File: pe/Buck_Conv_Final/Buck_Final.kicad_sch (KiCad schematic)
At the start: 11 parts, among them U1 BD95821MUV-E2

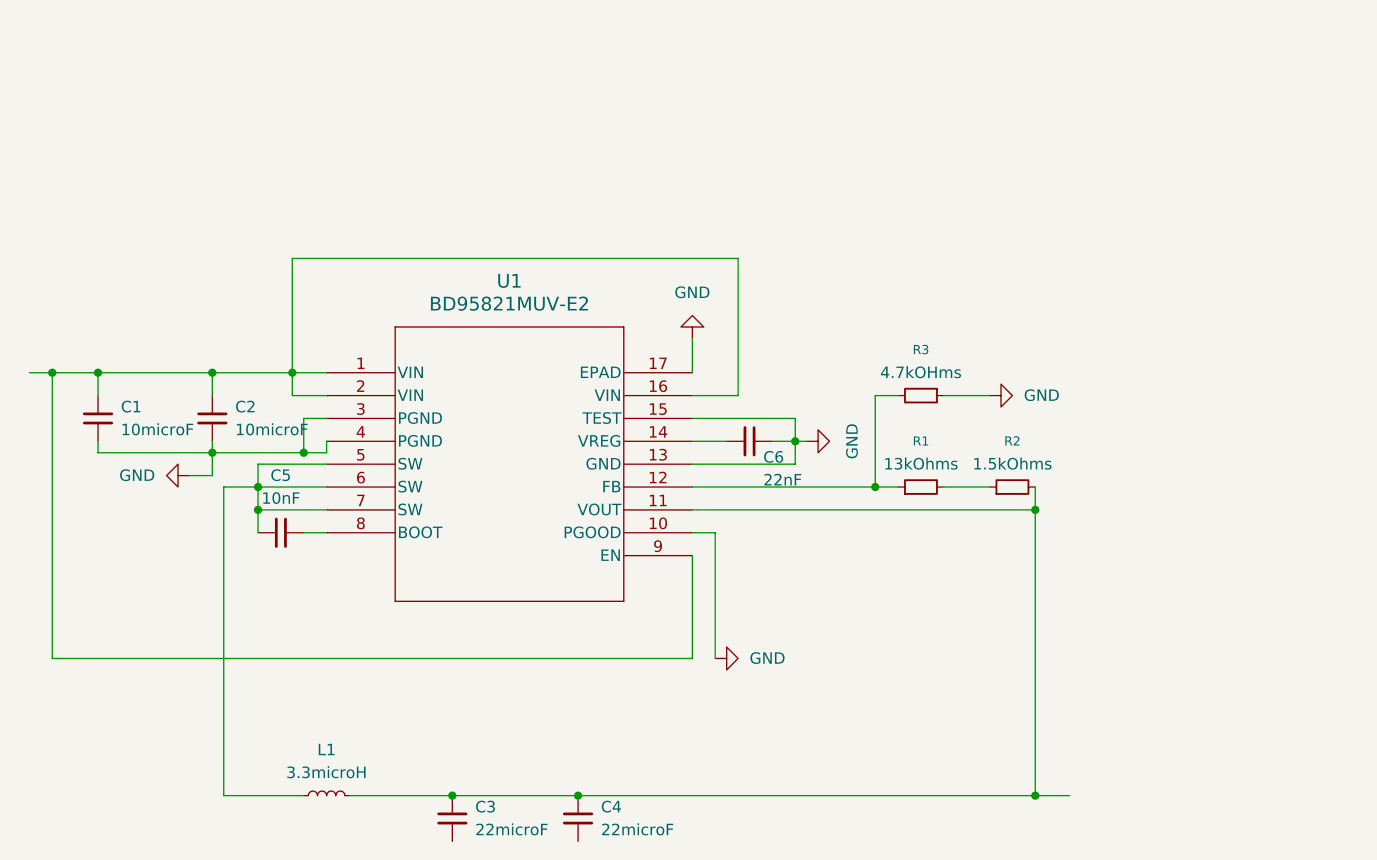
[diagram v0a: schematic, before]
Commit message: Buck Conv with TPS5405
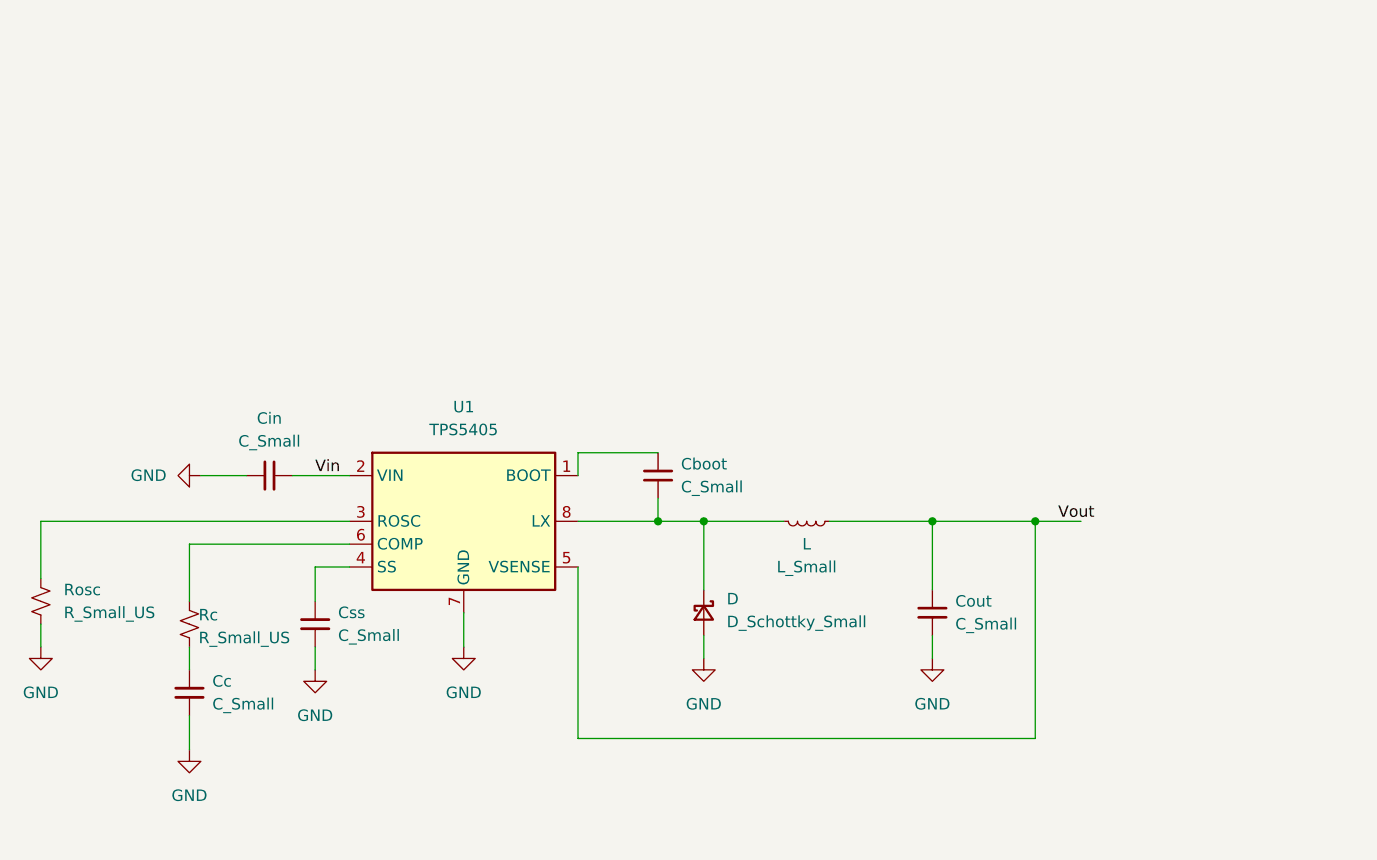
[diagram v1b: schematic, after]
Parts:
- removed C1, C2: 10microF, symbol Device:C_Small
- removed C3, C4: 22microF, symbol Device:C_Small
- removed C5: 10nF, symbol Device:C_Small
- removed C6: 22nF, symbol Device:C_Small
- removed L1: 3.3microH, symbol Device:L_Small
- removed R1: 13kOhms, symbol Device:R_Small
- removed R2: 1.5kOhms, symbol Device:R_Small
- removed R3: 4.7kOHms, symbol Device:R_Small
- removed U1: BD95821MUV-E2, BD95821MUV:VQFN016V3030_ROM, symbol BD95821MUV:BD95821MUV-E2
- added Cboot, Cc, Cin, Cout, Css: C_Small, symbol Device:C_Small
- added D: D_Schottky_Small, symbol Device:D_Schottky_Small
- added L: L_Small, symbol Device:L_Small
- added Rc, Rosc: R_Small_US, Resistor_THT:R_Array_SIP4, symbol Device:R_Small_US
- added U1: TPS5405, Package_SO:SOIC-8_3.9x4.9mm_P1.27mm, symbol Regulator_Switching:TPS5403
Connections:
- net GND: now also Cc.1, Cin.1, Cout.2, Css.1, D.2 (A), Rosc.2, U1.7 (GND)
- new net: Cboot.1, D.1 (K), L.2, U1.8 (LX)
- new net: Cboot.2, U1.1 (BOOT)
- new net: Rc.1, U1.6 (COMP)
- new net: Cc.2, Rc.2
- new net: Rosc.1, U1.3 (ROSC)
- new net: Css.2, U1.4 (SS)
- new net Vin: Cin.2, U1.2 (VIN)
- new net Vout: Cout.1, L.1, U1.5 (VSENSE)
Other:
- title: Buck Converter -> ${BOARD_TITLE}

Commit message: Schematic Values and PCB Started
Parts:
- removed Cboot, Cc, Cout, Css: C_Small, symbol Device:C_Small
- removed D: D_Schottky_Small, symbol Device:D_Schottky_Small
- removed L: L_Small, symbol Device:L_Small
- removed Rc: R_Small_US, Resistor_THT:R_Array_SIP4, symbol Device:R_Small_US
- removed U1: TPS5405, Package_SO:SOIC-8_3.9x4.9mm_P1.27mm, symbol Regulator_Switching:TPS5403
- added Cboot1: 0.1microF, Capacitor_SMD:C_0603_1608Metric_Pad1.08x0.95mm_HandSolder, symbol Device:C_Small
- added Cc1: 2.2nF, Capacitor_SMD:C_0603_1608Metric_Pad1.08x0.95mm_HandSolder, symbol Device:C_Small
- added Cout1: 100microF, Capacitor_SMD:C_0603_1608Metric_Pad1.08x0.95mm_HandSolder, symbol Device:C_Small
- added Css1: 5nF, Capacitor_SMD:C_0603_1608Metric_Pad1.08x0.95mm_HandSolder, symbol Device:C_Small
- added D1: D_Schottky_Small, Diode_SMD:D_0603_1608Metric_Pad1.05x0.95mm_HandSolder, symbol Device:D_Schottky_Small
- added L1: 10microH, Inductor_SMD:L_0603_1608Metric_Pad1.05x0.95mm_HandSolder, symbol Device:L_Small
- added Rc1: 10kOhms, Resistor_SMD:R_0603_1608Metric_Pad0.98x0.95mm_HandSolder, symbol Device:R_Small_US
- added U2: TPS5405DR, TPS5405DR:D0008A-IPC_A, symbol TPS5405DR:TPS5405DR
- Cin1: renamed from Cin; value C_Small -> 22microF; footprint (none) -> Capacitor_SMD:C_0603_1608Metric_Pad1.08x0.95mm_HandSolder
- Rosc1: renamed from Rosc; value R_Small_US -> 49.9kohms; footprint Resistor_THT:R_Array_SIP4 -> Resistor_SMD:R_0603_1608Metric_Pad0.98x0.95mm_HandSolder
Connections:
- net GND: now also Cc1.1, Cout1.2, Css1.1, D1.2 (A), U2.7 (GND)
- net Vin: now also U2.2 (VIN)
- net Vout: now also Cout1.1, L1.1, U2.5 (VSENSE)
- net at Rosc1.1: now also U2.3 (ROSC)
- new net: Cboot1.1, D1.1 (K), L1.2, U2.8 (LX)
- new net: Rc1.1, U2.6 (COMP)
- new net: Cc1.2, Rc1.2
- new net: Cboot1.2, U2.1 (BOOT)
- new net: Css1.2, U2.4 (SS)
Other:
- title: ${BOARD_TITLE} -> 12-5 Buck Converter
- moved on the sheet: Cin1, Rosc1

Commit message: Diode Rename
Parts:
- D1: value D_Schottky_Small -> (none)
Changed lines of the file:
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@@
 			)
 		)
-		(property "Value" "D_Schottky_Small"
+		(property "Value" ""
 			(at 190.5 63.2459 90)
 			(show_name no)
@@
 			(at 187.96 62.23 0)
 			(hide yes)
+			(show_name no)
+			(do_not_autoplace no)
+			(effects
+				(font
+					(size 1.27 1.27)
+				)
+			)
+		)
+		(property "Digikey Part Number" ""
+			(at 187.96 62.23 0)
+			(hide yes)
+			(show_name no)
+			(do_not_autoplace no)
+			(effects
+				(font
+					(size 1.27 1.27)
+				)
+			)
+		)
+		(property "Digikey URL" ""
+			(at 187.96 62.23 0)
+			(hide yes)
+			(show_name no)
+			(do_not_autoplace no)
+			(effects
+				(font
+					(size 1.27 1.27)
+				)
+			)
+		)
+		(property "Manufacturer" ""
+			(at 187.96 62.23 0)
+			(hide yes)
+			(show_name no)
+			(do_not_autoplace no)
+			(effects
+				(font
+					(size 1.27 1.27)
+				)
+			)
+		)
+		(property "Manufacturer Part Number" ""
+			(at 187.96 62.23 0)
+			(hide yes)

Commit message: Library for buck IC, math for components, minor updates
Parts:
- added Vin1: Conn_01x02, Connector_PinHeader_1.00mm:PinHeader_1x02_P1.00mm_Vertical, symbol Connector_Generic:Conn_01x02
- added Vout1: (no value), Connector_PinHeader_1.00mm:PinHeader_1x02_P1.00mm_Vertical, symbol Connector_Generic:Conn_01x02
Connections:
- net GND: now also Vin1.1 (Pin_1), Vout1.2 (Pin_2)
- net Vin: now also Vin1.2 (Pin_2)
- net Vout: now also Vout1.1 (Pin_1)
